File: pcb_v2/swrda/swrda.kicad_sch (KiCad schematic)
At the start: 22 parts, among them U1 74LS138, U10 74LS32, U12 74LS02, U2 74LS138, U3 74LS138, U4 74LS138, U5 74LS04, U6 74LS08, U7 74LS00, U8 74LS138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

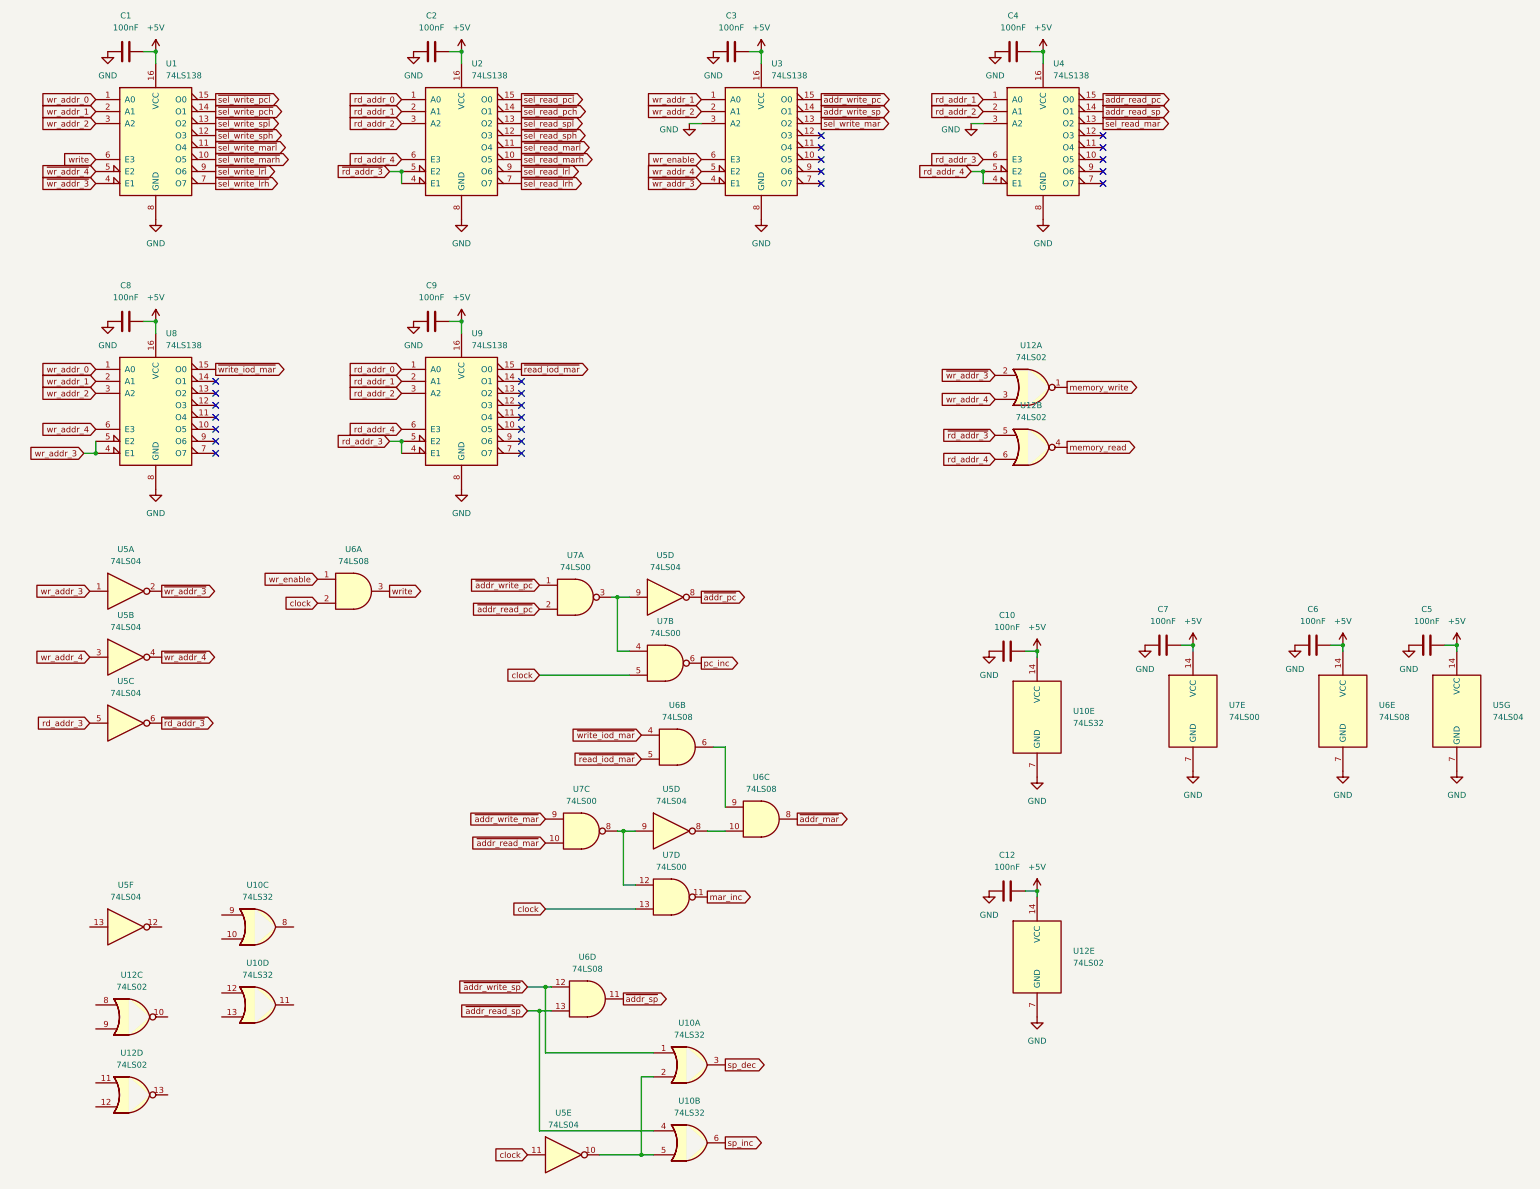
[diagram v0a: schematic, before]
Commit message: alterando os pinos de alimentacao no conector
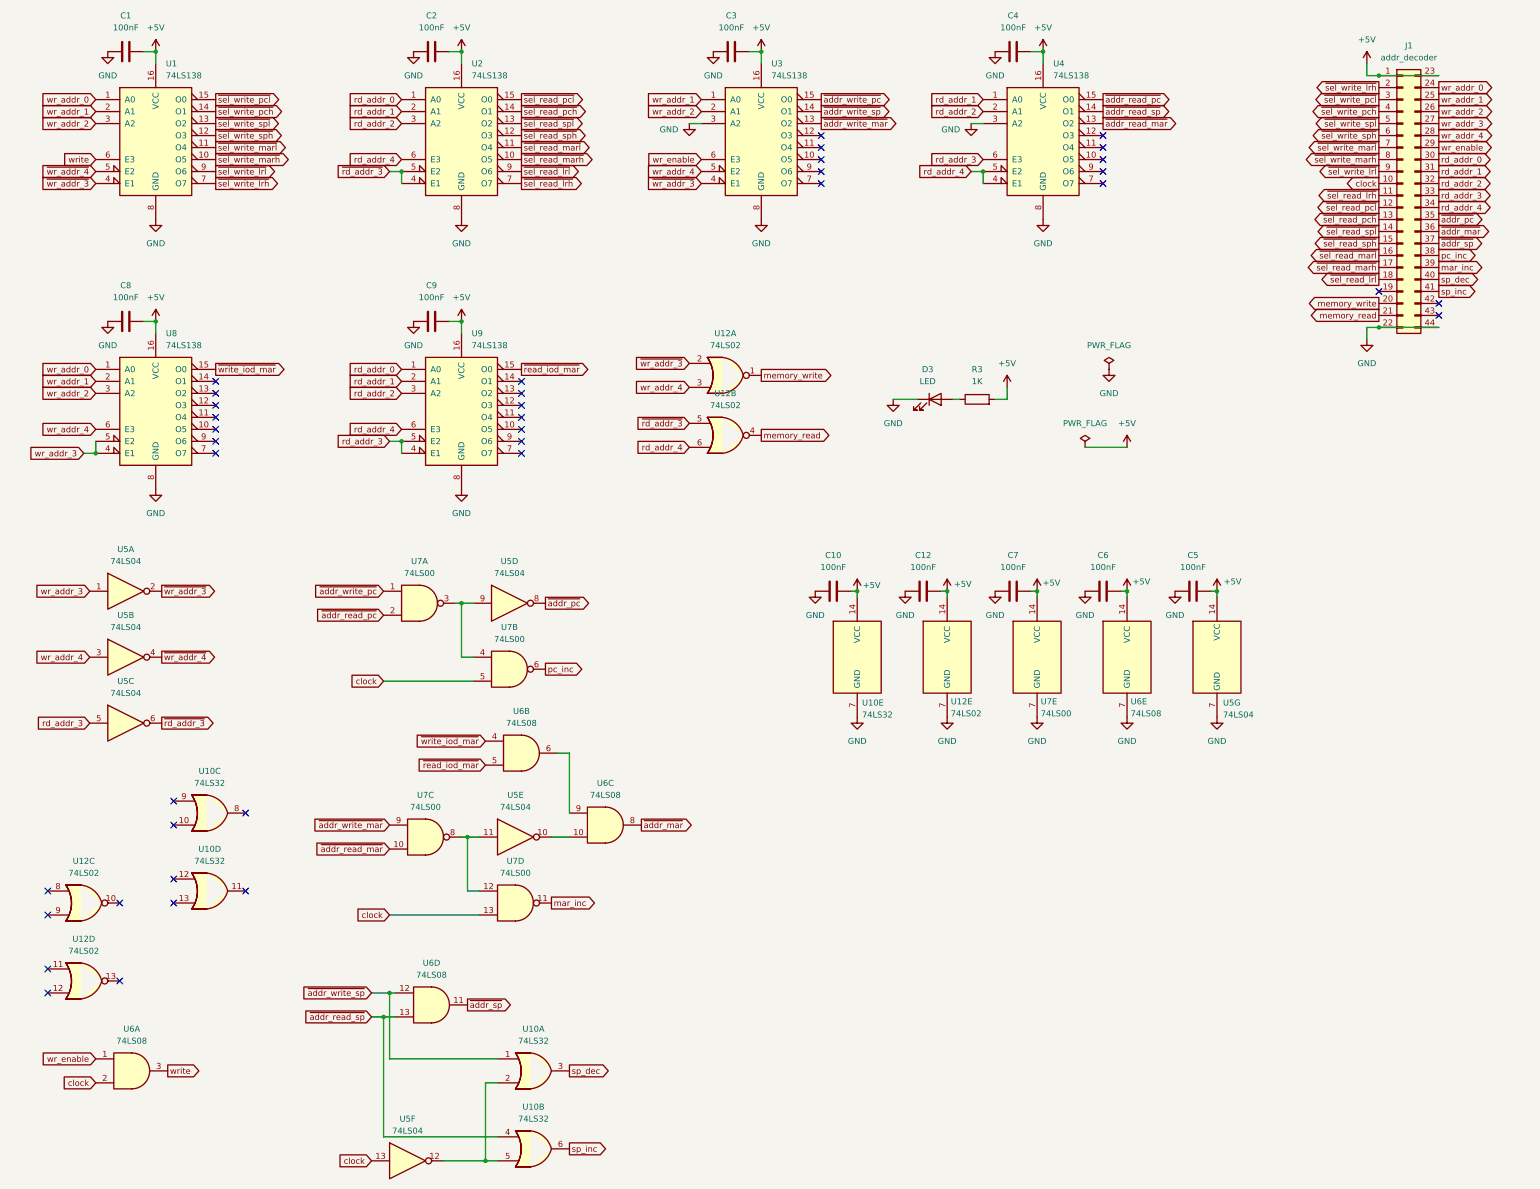
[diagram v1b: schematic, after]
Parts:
- removed unit 6 of U5
- added D3: LED, LED_THT:LED_D5.0mm, symbol Device:LED
- added J1: addr_decoder, edge_connector:edge-connector-44, symbol Connector_Generic:Conn_02x22_Top_Bottom
- added R3: 1K, Resistor_SMD:R_1206_3216Metric, symbol Device:R
- C1, C10, C12, C2, C3, C4, C5, C6, C7, C8, C9: footprint (none) -> Capacitor_SMD:C_1206_3216Metric
- U1, U2, U3, U4, U8, U9: footprint (none) -> Package_DIP:SMDIP-16_W7.62mm
- U10, U12, U5, U6, U7: footprint (none) -> Package_DIP:SMDIP-14_W7.62mm
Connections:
- net ~{sel_read_mar} is gone; now on net ~{addr_read_mar}: U4.13 (O2)
- net ~{sel_write_mar} is gone; now on net ~{addr_write_mar}: U3.13 (O2)
- net +5V: now also J1.1 (Pin_1), J1.23 (Pin_23), R3.2
- net GND: now also D3.1 (K), J1.22 (Pin_22), J1.44 (Pin_44)
- net clock: now also U5.13, J1.10 (Pin_10); no longer U5.11
- net mar_inc: now also J1.39 (Pin_39)
- net memory_read: now also J1.21 (Pin_21)
- net memory_write: now also J1.20 (Pin_20)
- net pc_inc: now also J1.38 (Pin_38)
- net rd_addr_0: now also J1.30 (Pin_30)
- net rd_addr_1: now also J1.31 (Pin_31)
- net rd_addr_2: now also J1.32 (Pin_32)
- net rd_addr_3: now also J1.33 (Pin_33)
- net rd_addr_4: now also J1.34 (Pin_34)
- net sp_dec: now also J1.40 (Pin_40)
- net sp_inc: now also J1.41 (Pin_41)
- net wr_addr_0: now also J1.24 (Pin_24)
- net wr_addr_1: now also J1.25 (Pin_25)
- net wr_addr_2: now also J1.26 (Pin_26)
- net wr_addr_3: now also J1.27 (Pin_27)
- net wr_addr_4: now also J1.28 (Pin_28)
- net wr_enable: now also J1.29 (Pin_29)
- net ~{addr_mar}: now also J1.36 (Pin_36)
- net ~{addr_pc}: now also J1.35 (Pin_35)
- net ~{addr_sp}: now also J1.37 (Pin_37)
- net ~{sel_read_lrh}: now also J1.11 (Pin_11)
- net ~{sel_read_lrl}: now also J1.18 (Pin_18)
- net ~{sel_read_marh}: now also J1.17 (Pin_17)
- net ~{sel_read_marl}: now also J1.16 (Pin_16)
- net ~{sel_read_pch}: now also J1.13 (Pin_13)
- net ~{sel_read_pcl}: now also J1.12 (Pin_12)
- net ~{sel_read_sph}: now also J1.15 (Pin_15)
- net ~{sel_read_spl}: now also J1.14 (Pin_14)
- net ~{sel_write_lrh}: now also J1.2 (Pin_2)
- net ~{sel_write_lrl}: now also J1.9 (Pin_9)
- net ~{sel_write_marh}: now also J1.8 (Pin_8)
- net ~{sel_write_marl}: now also J1.7 (Pin_7)
- net ~{sel_write_pch}: now also J1.4 (Pin_4)
- net ~{sel_write_pcl}: now also J1.3 (Pin_3)
- net ~{sel_write_sph}: now also J1.6 (Pin_6)
- net ~{sel_write_spl}: now also J1.5 (Pin_5)
- net at U10.2, U10.5: now also U5.12; no longer U5.10
- net at U6.10: now also U5.10; no longer U5.8
- net at U7.12, U7.8: now also U5.11; no longer U5.9
- new net: D3.2 (A), R3.1
- no-connect marks 24 -> 39
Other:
- moved on the sheet: C10, C12, C5, C6, C7, U10A, U10B, U10C, U10D, U10E, U12A, U12B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

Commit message: concluido o desenho das placas satelite do banco de registradores de 16 bits
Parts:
- C1, C10, C12, C2, C3, C4, C5, C6, C7, C8, C9: footprint Capacitor_SMD:C_1206_3216Metric -> Capacitor_THT:C_Disc_D5.1mm_W3.2mm_P5.00mm
- D3: value LED -> PWR
- R3: footprint Resistor_SMD:R_1206_3216Metric -> Resistor_THT:R_Axial_DIN0207_L6.3mm_D2.5mm_P7.62mm_Horizontal
- U1, U2, U3, U4, U8, U9: footprint Package_DIP:SMDIP-16_W7.62mm -> Package_DIP:DIP-16_W7.62mm
- U10, U12, U5, U6, U7: footprint Package_DIP:SMDIP-14_W7.62mm -> Package_DIP:DIP-14_W7.62mm
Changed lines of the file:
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@@
 			)
 		)
-		(property "Footprint" "Package_DIP:SMDIP-14_W7.62mm"
+		(property "Footprint" "Package_DIP:DIP-14_W7.62mm"
 			(at 123.19 256.54 0)
 			(effects
@@
 			)
 		)
-		(property "Footprint" "Package_DIP:SMDIP-16_W7.62mm"
+		(property "Footprint" "Package_DIP:DIP-16_W7.62mm"
 			(at 43.18 41.91 0)
 			(effects
@@
 			)
 		)
-		(property "Footprint" "Package_DIP:SMDIP-14_W7.62mm"
+		(property "Footprint" "Package_DIP:DIP-14_W7.62mm"
 			(at 163.83 105.41 0)
 			(effects
@@
 			)
 		)
-		(property "Value" "LED"
+		(property "Value" "PWR"
 			(at 206.6925 93.98 0)
 			(effects
@@
 			)
 		)
-		(property "Footprint" "Package_DIP:SMDIP-14_W7.62mm"
+		(property "Footprint" "Package_DIP:DIP-14_W7.62mm"
 			(at 138.43 187.96 0)
 			(effects
@@
 			)
 		)
-		(property "Footprint" "Package_DIP:SMDIP-14_W7.62mm"
+		(property "Footprint" "Package_DIP:DIP-14_W7.62mm"
 			(at 38.1 240.03 0)
 			(effects
@@
 			)
 		)
-		(property "Footprint" "Package_DIP:SMDIP-14_W7.62mm"
+		(property "Footprint" "Package_DIP:DIP-14_W7.62mm"
 			(at 163.83 92.71 0)
 			(effects
@@
 			)
 		)
-		(property "Footprint" "Capacitor_SMD:C_1206_3216Metric"
+		(property "Footprint" "Capacitor_THT:C_Disc_D5.1mm_W3.2mm_P5.00mm"
 			(at 168.91 23.1648 0)
 			(effects
@@
 			)
 		)
-		(property "Footprint" "Capacitor_SMD:C_1206_3216Metric"
+		(property "Footprint" "Capacitor_THT:C_Disc_D5.1mm_W3.2mm_P5.00mm"
 			(at 247.65 137.4648 0)
 			(effects
@@
 			)
 		)
-		(property "Footprint" "Package_DIP:SMDIP-16_W7.62mm"
+		(property "Footprint" "Package_DIP:DIP-16_W7.62mm"
 			(at 231.14 41.91 0)
 			(effects
@@
 			)
 		)
-		(property "Footprint" "Package_DIP:SMDIP-14_W7.62mm"
+		(property "Footprint" "Package_DIP:DIP-14_W7.62mm"
 			(at 191.77 152.4 0)
 			(effects
@@
 			)
 		)
-		(property "Footprint" "Package_DIP:SMDIP-14_W7.62mm"
+		(property "Footprint" "Package_DIP:DIP-14_W7.62mm"
 			(at 36.83 152.4 0)
 			(effects
@@
 			)
 		)
-		(property "Footprint" "Package_DIP:SMDIP-14_W7.62mm"
+		(property "Footprint" "Package_DIP:DIP-14_W7.62mm"
 			(at 101.6 226.06 0)
 			(effects
@@
 			)
 		)
-		(property "Footprint" "Package_DIP:SMDIP-14_W7.62mm"
+		(property "Footprint" "Package_DIP:DIP-14_W7.62mm"
 			(at 118.11 140.97 0)
 			(effects
@@
 			)
 		)
-		(property "Footprint" "Capacitor_SMD:C_1206_3216Metric"
+		(property "Footprint" "Capacitor_THT:C_Disc_D5.1mm_W3.2mm_P5.00mm"
 			(at 40.64 23.1648 0)
 			(effects
@@
 			)
 		)
-		(property "Footprint" "Capacitor_SMD:C_1206_3216Metric"
+		(property "Footprint" "Capacitor_THT:C_Disc_D5.1mm_W3.2mm_P5.00mm"
 			(at 105.41 80.3148 0)
 			(effects
@@
 			)
 		)
-		(property "Footprint" "Package_DIP:SMDIP-14_W7.62mm"
+		(property "Footprint" "Package_DIP:DIP-14_W7.62mm"
 			(at 54.61 201.93 0)
 			(effects
@@
 			)
 		)
-		(property "Footprint" "Capacitor_SMD:C_1206_3216Metric"
+		(property "Footprint" "Capacitor_THT:C_Disc_D5.1mm_W3.2mm_P5.00mm"
 			(at 40.64 80.3148 0)
 			(effects
@@
 			)
 		)
-		(property "Footprint" "Package_DIP:SMDIP-14_W7.62mm"
+		(property "Footprint" "Package_DIP:DIP-14_W7.62mm"
 			(at 100.33 190.5 0)
 			(effects
@@
 			)
 		)
-		(property "Footprint" "Package_DIP:SMDIP-14_W7.62mm"
+		(property "Footprint" "Package_DIP:DIP-14_W7.62mm"
 			(at 27.94 220.98 0)
 			(effects
@@
 			)
 		)
-		(property "Footprint" "Capacitor_SMD:C_1206_3216Metric"
+		(property "Footprint" "Capacitor_THT:C_Disc_D5.1mm_W3.2mm_P5.00mm"
 			(at 209.55 137.4648 0)
 			(effects
@@
 			)
 		)
-		(property "Footprint" "Capacitor_SMD:C_1206_3216Metric"
+		(property "Footprint" "Capacitor_THT:C_Disc_D5.1mm_W3.2mm_P5.00mm"
 			(at 228.6 23.1648 0)
 			(effects
@@
 			)
 		)
-		(property "Footprint" "Resistor_SMD:R_1206_3216Metric"
+		(property "Footprint" "Resistor_THT:R_Axial_DIN0207_L6.3mm_D2.5mm_P7.62mm_Horizontal"
 			(at 217.17 99.568 90)
 			(effects
@@
 			)
 		)
-		(property "Footprint" "Package_DIP:SMDIP-14_W7.62mm"
+		(property "Footprint" "Package_DIP:DIP-14_W7.62mm"
 			(at 210.82 152.4 0)
 			(effects
@@
 			)
 		)
-		(property "Footprint" "Package_DIP:SMDIP-14_W7.62mm"
+		(property "Footprint" "Package_DIP:DIP-14_W7.62mm"
 			(at 36.83 138.43 0)
 			(effects
@@
 			)
 		)
-		(property "Footprint" "Package_DIP:SMDIP-16_W7.62mm"
+		(property "Footprint" "Package_DIP:DIP-16_W7.62mm"
 			(at 43.18 99.06 0)
 			(effects
@@
 			)
 		)
-		(property "Footprint" "Package_DIP:SMDIP-14_W7.62mm"
+		(property "Footprint" "Package_DIP:DIP-14_W7.62mm"
 			(at 120.65 172.72 0)
 			(effects
@@
 			)
 		)
-		(property "Footprint" "Package_DIP:SMDIP-14_W7.62mm"
+		(property "Footprint" "Package_DIP:DIP-14_W7.62mm"
 			(at 96.52 259.08 0)
 			(effects
@@
 			)
 		)
-		(property "Footprint" "Package_DIP:SMDIP-14_W7.62mm"
+		(property "Footprint" "Package_DIP:DIP-14_W7.62mm"
 			(at 27.94 204.47 0)
 			(effects
@@
 			)
 		)
-		(property "Footprint" "Package_DIP:SMDIP-14_W7.62mm"
+		(property "Footprint" "Package_DIP:DIP-14_W7.62mm"
 			(at 248.92 152.4 0)
 			(effects
@@
 			)
 		)
-		(property "Footprint" "Package_DIP:SMDIP-16_W7.62mm"
+		(property "Footprint" "Package_DIP:DIP-16_W7.62mm"
 			(at 171.45 41.91 0)
 			(effects
@@
 			)
 		)
-		(property "Footprint" "Package_DIP:SMDIP-16_W7.62mm"
+		(property "Footprint" "Package_DIP:DIP-16_W7.62mm"
 			(at 107.95 41.91 0)
 			(effects
@@
 			)
 		)
-		(property "Footprint" "Package_DIP:SMDIP-14_W7.62mm"
+		(property "Footprint" "Package_DIP:DIP-14_W7.62mm"
 			(at 119.38 190.5 0)
 			(effects
@@
 			)
 		)
-		(property "Footprint" "Package_DIP:SMDIP-14_W7.62mm"
+		(property "Footprint" "Package_DIP:DIP-14_W7.62mm"
 			(at 119.38 204.47 0)
 			(effects
@@
 			)
 		)
-		(property "Footprint" "Capacitor_SMD:C_1206_3216Metric"
+		(property "Footprint" "Capacitor_THT:C_Disc_D5.1mm_W3.2mm_P5.00mm"
 			(at 228.6 137.4648 0)
 			(effects
@@
 			)
 		)
-		(property "Footprint" "Package_DIP:SMDIP-14_W7.62mm"
+		(property "Footprint" "Package_DIP:DIP-14_W7.62mm"
 			(at 267.97 152.4 0)
 			(effects
@@
 			)
 		)
-		(property "Footprint" "Package_DIP:SMDIP-14_W7.62mm"
+		(property "Footprint" "Package_DIP:DIP-14_W7.62mm"
 			(at 123.19 240.03 0)
 			(effects
@@
 			)
 		)
-		(property "Footprint" "Capacitor_SMD:C_1206_3216Metric"
+		(property "Footprint" "Capacitor_THT:C_Disc_D5.1mm_W3.2mm_P5.00mm"
 			(at 266.7 137.4648 0)
 			(effects
@@
 			)
 		)
-		(property "Footprint" "Package_DIP:SMDIP-14_W7.62mm"
+		(property "Footprint" "Package_DIP:DIP-14_W7.62mm"
 			(at 99.06 140.97 0)
 			(effects
@@
 			)
 		)
-		(property "Footprint" "Package_DIP:SMDIP-14_W7.62mm"
+		(property "Footprint" "Package_DIP:DIP-14_W7.62mm"
 			(at 118.11 154.94 0)
 			(effects
@@
 			)
 		)
-		(property "Footprint" "Package_DIP:SMDIP-14_W7.62mm"
+		(property "Footprint" "Package_DIP:DIP-14_W7.62mm"
 			(at 54.61 185.42 0)
 			(effects
@@
 			)
 		)
-		(property "Footprint" "Capacitor_SMD:C_1206_3216Metric"
+		(property "Footprint" "Capacitor_THT:C_Disc_D5.1mm_W3.2mm_P5.00mm"
 			(at 105.41 23.1648 0)
 			(effects
@@
 			)
 		)
-		(property "Footprint" "Package_DIP:SMDIP-16_W7.62mm"
+		(property "Footprint" "Package_DIP:DIP-16_W7.62mm"
 			(at 107.95 99.06 0)
 			(effects
@@
 			)
 		)
-		(property "Footprint" "Capacitor_SMD:C_1206_3216Metric"
+		(property "Footprint" "Capacitor_THT:C_Disc_D5.1mm_W3.2mm_P5.00mm"
 			(at 190.5 137.4648 0)
 			(effects
@@
 			)
 		)
-		(property "Footprint" "Package_DIP:SMDIP-14_W7.62mm"
+		(property "Footprint" "Package_DIP:DIP-14_W7.62mm"
 			(at 229.87 152.4 0)
 			(effects
@@
 			)
 		)
-		(property "Footprint" "Package_DIP:SMDIP-14_W7.62mm"
+		(property "Footprint" "Package_DIP:DIP-14_W7.62mm"
 			(at 36.83 166.37 0)
 			(effects
